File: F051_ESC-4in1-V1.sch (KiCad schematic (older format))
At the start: 39 parts, among them J1 Conn_01x02, J11 Conn_01x03, J14 Conn_01x03, J2 Conn_01x10, J3 Conn_01x05, J4 Conn_01x05, J5 Conn_01x05, J6 Conn_01x03, J7 Conn_01x05, J8 Conn_01x03, J9 Conn_01x10

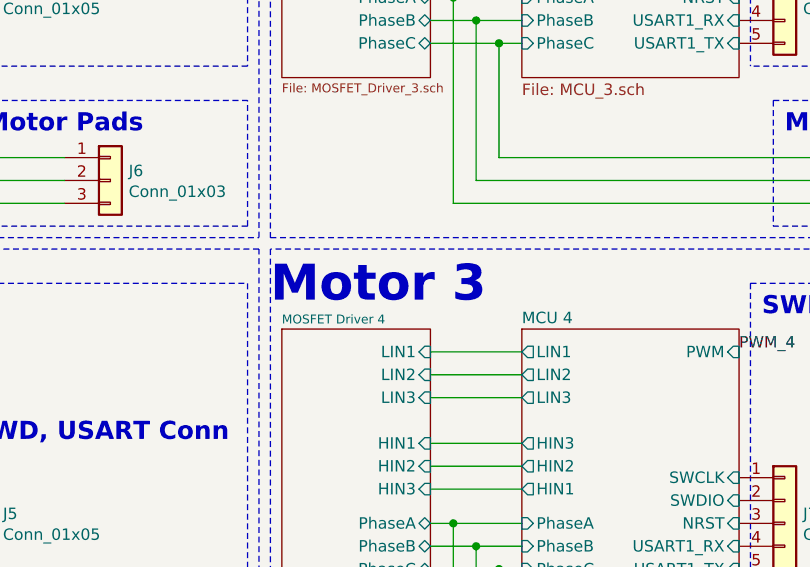
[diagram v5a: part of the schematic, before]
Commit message: Finished all traces and vias
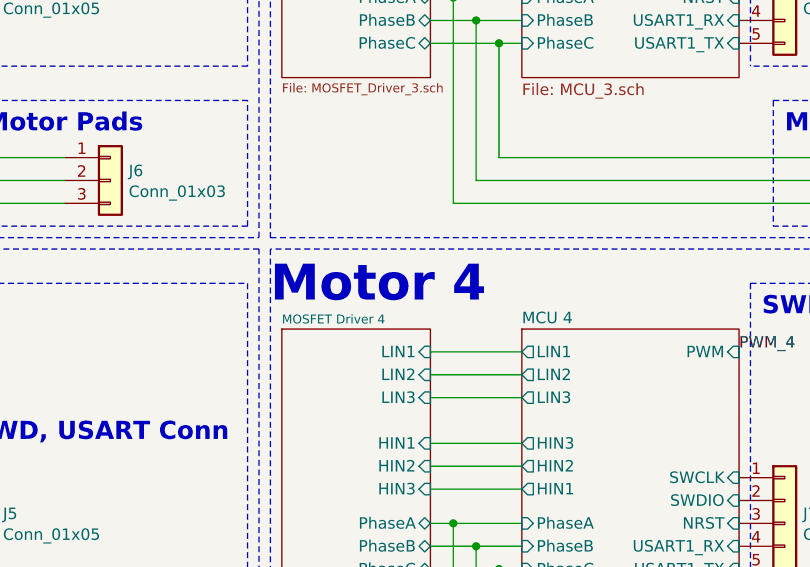
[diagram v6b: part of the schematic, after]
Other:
- note added: "Motor 4"
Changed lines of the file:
@@
 	11150 5100 11150 2850
 Text Notes 7700 3100 0    157  ~ 31
-Motor 3
+Motor 4
 Wire Wire Line
 	8500 4950 10300 4950

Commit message: Added more PNGs
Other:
- note removed: "5V SMPS"
- moved on the sheet: C16, C17, C18, C19, C20, C21, C50, C51, C52, C53, C54, C55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

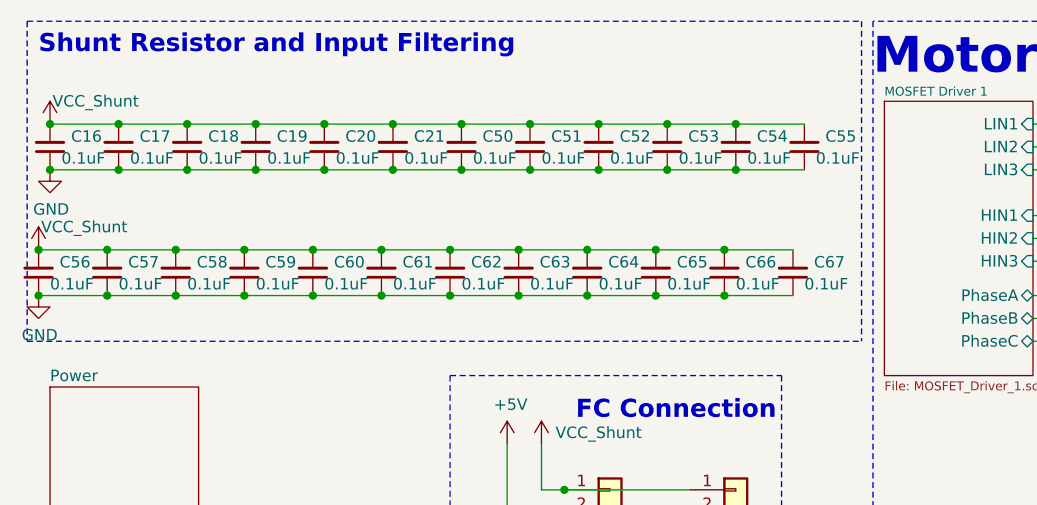
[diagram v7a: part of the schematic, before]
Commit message: Changed input filtering caps to 47uF from 0.1uF
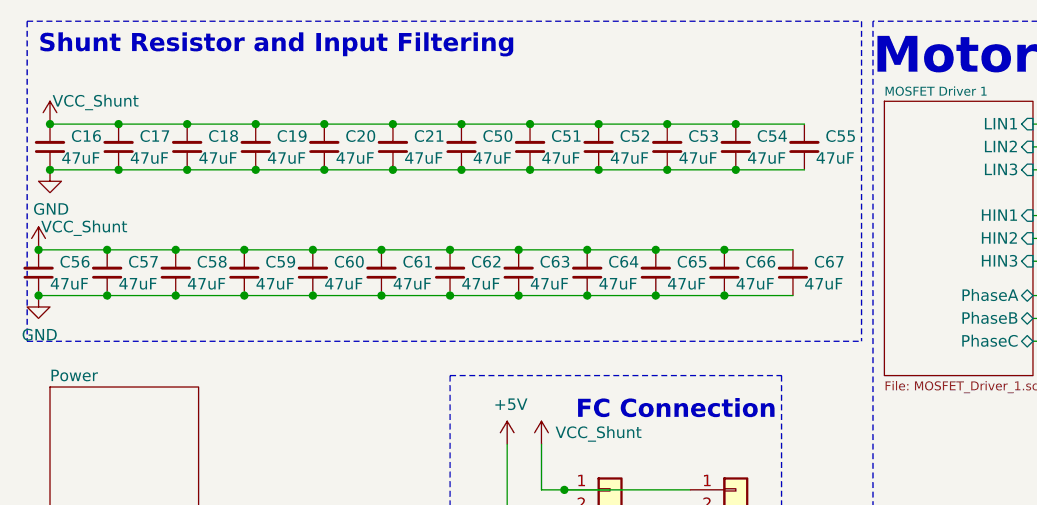
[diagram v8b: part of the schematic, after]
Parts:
- C16, C17, C18, C19, C20, C21, C50, C51, C52, C53, C54, C55, C56, C57, C58, C59, C60, C61, C62, C63, C64, C65, C66, C67: value 0.1uF -> 47uF
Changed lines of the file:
@@
 P 600 1100
 F 0 "C16" H 508 1054 50  0000 R CNN
-F 1 "0.1uF" H 550 1150 50  0000 R CNN
+F 1 "47uF" H 550 1150 50  0000 R CNN
 F 2 "Capacitor_SMD:C_1206_3216Metric" H 600 1100 50  0001 C CNN
 F 3 "~" H 600 1100 50  0001 C CNN
@@
 P 900 1100
 F 0 "C17" H 808 1054 50  0000 R CNN
-F 1 "0.1uF" H 850 1150 50  0000 R CNN
+F 1 "47uF" H 850 1150 50  0000 R CNN
 F 2 "Capacitor_SMD:C_1206_3216Metric" H 900 1100 50  0001 C CNN
 F 3 "~" H 900 1100 50  0001 C CNN
@@
 P 1200 1100
 F 0 "C18" H 1108 1054 50  0000 R CNN
-F 1 "0.1uF" H 1150 1150 50  0000 R CNN
+F 1 "47uF" H 1150 1150 50  0000 R CNN
 F 2 "Capacitor_SMD:C_1206_3216Metric" H 1200 1100 50  0001 C CNN
 F 3 "~" H 1200 1100 50  0001 C CNN
@@
 P 1500 1100
 F 0 "C19" H 1408 1054 50  0000 R CNN
-F 1 "0.1uF" H 1450 1150 50  0000 R CNN
+F 1 "47uF" H 1450 1150 50  0000 R CNN
 F 2 "Capacitor_SMD:C_1206_3216Metric" H 1500 1100 50  0001 C CNN
 F 3 "~" H 1500 1100 50  0001 C CNN
@@
 P 1800 1100
 F 0 "C20" H 1708 1054 50  0000 R CNN
-F 1 "0.1uF" H 1750 1150 50  0000 R CNN
+F 1 "47uF" H 1750 1150 50  0000 R CNN
 F 2 "Capacitor_SMD:C_1206_3216Metric" H 1800 1100 50  0001 C CNN
 F 3 "~" H 1800 1100 50  0001 C CNN
@@
 P 2100 1100
 F 0 "C21" H 2008 1054 50  0000 R CNN
-F 1 "0.1uF" H 2050 1150 50  0000 R CNN
+F 1 "47uF" H 2050 1150 50  0000 R CNN
 F 2 "Capacitor_SMD:C_1206_3216Metric" H 2100 1100 50  0001 C CNN
 F 3 "~" H 2100 1100 50  0001 C CNN
@@
 P 2400 1100
 F 0 "C50" H 2308 1054 50  0000 R CNN
-F 1 "0.1uF" H 2350 1150 50  0000 R CNN
+F 1 "47uF" H 2350 1150 50  0000 R CNN
 F 2 "Capacitor_SMD:C_1206_3216Metric" H 2400 1100 50  0001 C CNN
 F 3 "~" H 2400 1100 50  0001 C CNN
@@
 P 2700 1100
 F 0 "C51" H 2608 1054 50  0000 R CNN
-F 1 "0.1uF" H 2650 1150 50  0000 R CNN
+F 1 "47uF" H 2650 1150 50  0000 R CNN
 F 2 "Capacitor_SMD:C_1206_3216Metric" H 2700 1100 50  0001 C CNN
 F 3 "~" H 2700 1100 50  0001 C CNN
@@
 P 3000 1100
 F 0 "C52" H 2908 1054 50  0000 R CNN
-F 1 "0.1uF" H 2950 1150 50  0000 R CNN
+F 1 "47uF" H 2950 1150 50  0000 R CNN
 F 2 "Capacitor_SMD:C_1206_3216Metric" H 3000 1100 50  0001 C CNN
 F 3 "~" H 3000 1100 50  0001 C CNN
@@
 P 3300 1100
 F 0 "C53" H 3208 1054 50  0000 R CNN
-F 1 "0.1uF" H 3250 1150 50  0000 R CNN
+F 1 "47uF" H 3250 1150 50  0000 R CNN
 F 2 "Capacitor_SMD:C_1206_3216Metric" H 3300 1100 50  0001 C CNN
 F 3 "~" H 3300 1100 50  0001 C CNN
@@
 P 3600 1100
 F 0 "C54" H 3508 1054 50  0000 R CNN
-F 1 "0.1uF" H 3550 1150 50  0000 R CNN
+F 1 "47uF" H 3550 1150 50  0000 R CNN
 F 2 "Capacitor_SMD:C_1206_3216Metric" H 3600 1100 50  0001 C CNN
 F 3 "~" H 3600 1100 50  0001 C CNN
@@
 P 3900 1100
 F 0 "C55" H 3808 1054 50  0000 R CNN
-F 1 "0.1uF" H 3850 1150 50  0000 R CNN
+F 1 "47uF" H 3850 1150 50  0000 R CNN
 F 2 "Capacitor_SMD:C_1206_3216Metric" H 3900 1100 50  0001 C CNN
 F 3 "~" H 3900 1100 50  0001 C CNN
@@
 P 550 1650
 F 0 "C56" H 458 1604 50  0000 R CNN
-F 1 "0.1uF" H 500 1700 50  0000 R CNN
+F 1 "47uF" H 500 1700 50  0000 R CNN
 F 2 "Capacitor_SMD:C_1206_3216Metric" H 550 1650 50  0001 C CNN
 F 3 "~" H 550 1650 50  0001 C CNN
@@
 P 850 1650
 F 0 "C57" H 758 1604 50  0000 R CNN
-F 1 "0.1uF" H 800 1700 50  0000 R CNN
+F 1 "47uF" H 800 1700 50  0000 R CNN
 F 2 "Capacitor_SMD:C_1206_3216Metric" H 850 1650 50  0001 C CNN
 F 3 "~" H 850 1650 50  0001 C CNN
@@
 P 1150 1650
 F 0 "C58" H 1058 1604 50  0000 R CNN
-F 1 "0.1uF" H 1100 1700 50  0000 R CNN
+F 1 "47uF" H 1100 1700 50  0000 R CNN
 F 2 "Capacitor_SMD:C_1206_3216Metric" H 1150 1650 50  0001 C CNN
 F 3 "~" H 1150 1650 50  0001 C CNN
@@
 P 1450 1650
 F 0 "C59" H 1358 1604 50  0000 R CNN
-F 1 "0.1uF" H 1400 1700 50  0000 R CNN
+F 1 "47uF" H 1400 1700 50  0000 R CNN
 F 2 "Capacitor_SMD:C_1206_3216Metric" H 1450 1650 50  0001 C CNN
 F 3 "~" H 1450 1650 50  0001 C CNN
@@
 P 1750 1650
 F 0 "C60" H 1658 1604 50  0000 R CNN
-F 1 "0.1uF" H 1700 1700 50  0000 R CNN
+F 1 "47uF" H 1700 1700 50  0000 R CNN
 F 2 "Capacitor_SMD:C_1206_3216Metric" H 1750 1650 50  0001 C CNN
 F 3 "~" H 1750 1650 50  0001 C CNN
@@
 P 2050 1650
 F 0 "C61" H 1958 1604 50  0000 R CNN
-F 1 "0.1uF" H 2000 1700 50  0000 R CNN
+F 1 "47uF" H 2000 1700 50  0000 R CNN
 F 2 "Capacitor_SMD:C_1206_3216Metric" H 2050 1650 50  0001 C CNN
 F 3 "~" H 2050 1650 50  0001 C CNN
@@
 P 2350 1650
 F 0 "C62" H 2258 1604 50  0000 R CNN
-F 1 "0.1uF" H 2300 1700 50  0000 R CNN
+F 1 "47uF" H 2300 1700 50  0000 R CNN
 F 2 "Capacitor_SMD:C_1206_3216Metric" H 2350 1650 50  0001 C CNN
 F 3 "~" H 2350 1650 50  0001 C CNN
@@
 P 2650 1650
 F 0 "C63" H 2558 1604 50  0000 R CNN
-F 1 "0.1uF" H 2600 1700 50  0000 R CNN
+F 1 "47uF" H 2600 1700 50  0000 R CNN
 F 2 "Capacitor_SMD:C_1206_3216Metric" H 2650 1650 50  0001 C CNN
 F 3 "~" H 2650 1650 50  0001 C CNN
@@
 P 2950 1650
 F 0 "C64" H 2858 1604 50  0000 R CNN
-F 1 "0.1uF" H 2900 1700 50  0000 R CNN
+F 1 "47uF" H 2900 1700 50  0000 R CNN
 F 2 "Capacitor_SMD:C_1206_3216Metric" H 2950 1650 50  0001 C CNN
 F 3 "~" H 2950 1650 50  0001 C CNN
@@
 P 3250 1650
 F 0 "C65" H 3158 1604 50  0000 R CNN
-F 1 "0.1uF" H 3200 1700 50  0000 R CNN
+F 1 "47uF" H 3200 1700 50  0000 R CNN
 F 2 "Capacitor_SMD:C_1206_3216Metric" H 3250 1650 50  0001 C CNN
 F 3 "~" H 3250 1650 50  0001 C CNN
@@
 P 3550 1650
 F 0 "C66" H 3458 1604 50  0000 R CNN
-F 1 "0.1uF" H 3500 1700 50  0000 R CNN
+F 1 "47uF" H 3500 1700 50  0000 R CNN
 F 2 "Capacitor_SMD:C_1206_3216Metric" H 3550 1650 50  0001 C CNN
 F 3 "~" H 3550 1650 50  0001 C CNN
@@
 P 3850 1650
 F 0 "C67" H 3758 1604 50  0000 R CNN
-F 1 "0.1uF" H 3800 1700 50  0000 R CNN
+F 1 "47uF" H 3800 1700 50  0000 R CNN
 F 2 "Capacitor_SMD:C_1206_3216Metric" H 3850 1650 50  0001 C CNN
 F 3 "~" H 3850 1650 50  0001 C CNN
